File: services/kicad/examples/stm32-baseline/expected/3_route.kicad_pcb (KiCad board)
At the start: 2 copper layers, 50.3 x 37.7 mm, 17 parts, among them J1 5V, U1 STM32F103C8T6, U2 AMS1117-3.3

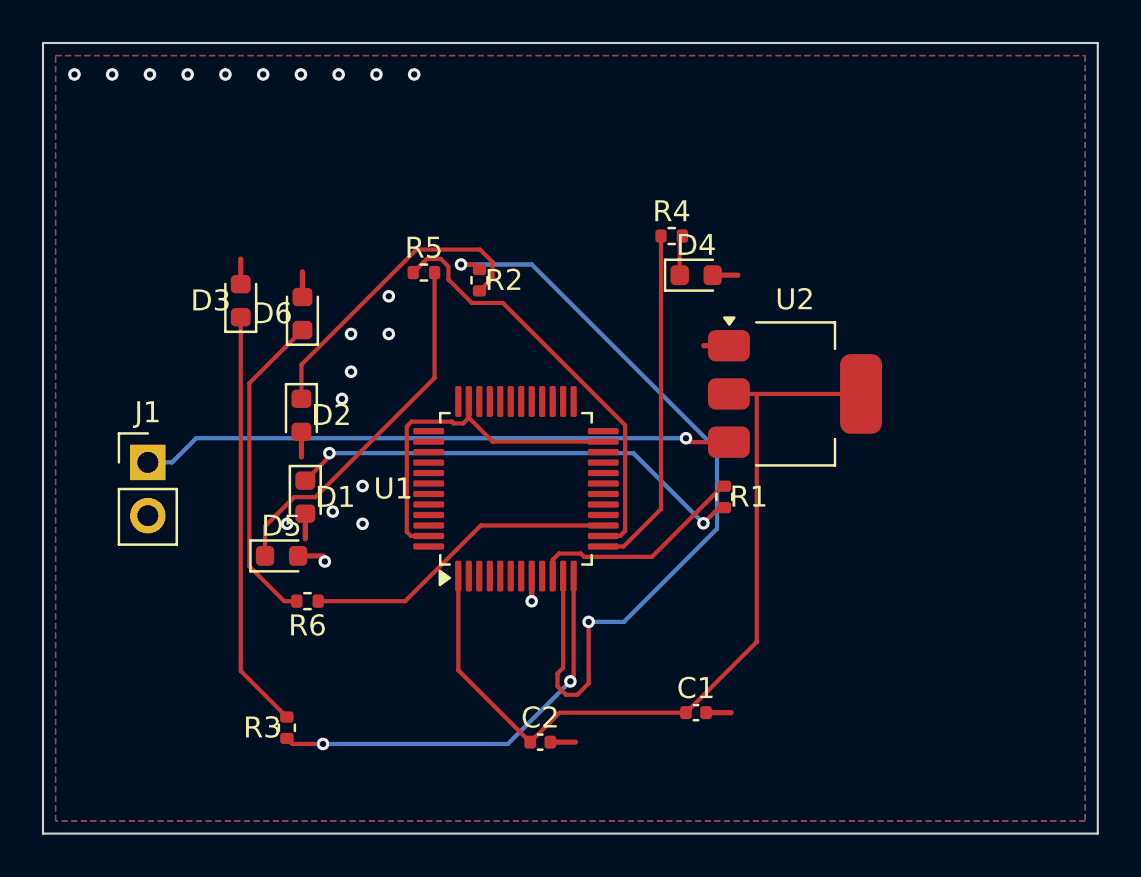
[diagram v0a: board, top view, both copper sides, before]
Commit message: feat(kicad): placement pro et routage 100 % fabricable sur les 16 cartes -- integration sur main (#164)
Branche d'integration coupee depuis origin/main (fab2a82, PR #162) : les
fichiers cles de main etaient des instantanes de feat/placement-seed-snap-
bypass (routing.py = 7981019, placement.py = 437a8b4...). On reprend donc
l'arbre entier de cette branche (345 commits, dernier 9f48667) et on y
conserve ce que main seul apportait :
- tools/verrou_routage.py + son test : « 6,2 Go par routage » rectifie
  (0,2 Go mesure ; c'est la concurrence qui emballe la memoire) ;
- tests/test_driver_llm_resync.py ;
- CLAUDE.md, PLAN.md, DECISIONS.md : fusion a trois voies, les sections
  des deux lignes conservees (2026-09-05 conteneur/verrou, 2026-09-07
  parcours asynchrone et chaine du driver, 2026-09-09/10 lecons).
Les skills *-delegate restent supprimes (remplaces le 2026-08-30).

Contenu : banc en deux phases (placement valide puis routage gele), snap
sur les regles natives, repli GND cible, journal Freerouting incremental,
horloge sans progres, via d'echappement vers le plan principal,
serigraphie degagee ; 16 cartes livrees a 100 %, 0 erreur DRC.

Verification : pytest services/kicad 1805 passed, 16 skipped ;
pnpm type-check 8/8.


Claude-Session: https://claude.ai/code/session_01TnMqm4La2CxQHHB5K8aSSV

Co-authored-by: Claude Fable 5.1 <noreply@anthropic.com>
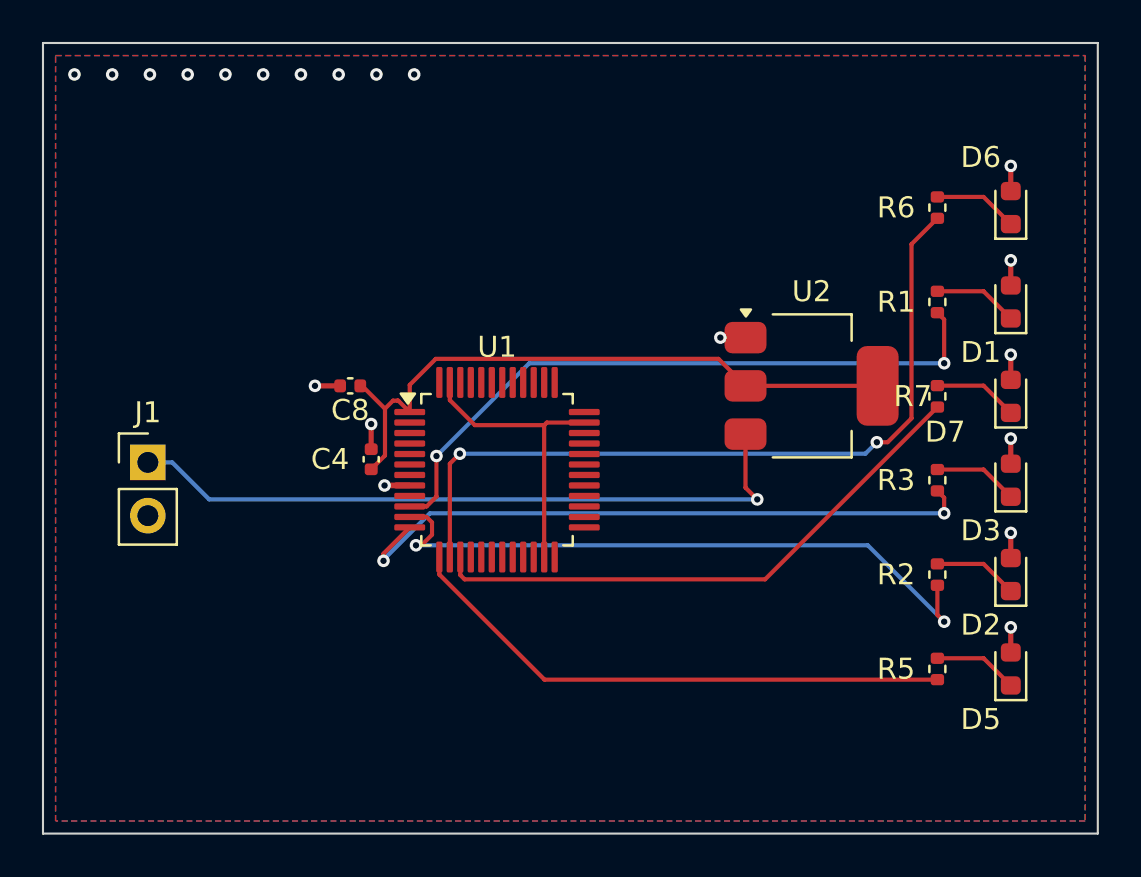
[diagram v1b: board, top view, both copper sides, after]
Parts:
- removed C1, C2: 100nF, C_0402_1005Metric
- removed D4: LED, LED_0603_1608Metric
- removed R4: 330, R_0402_1005Metric
- added C4: 100nF, C_0402_1005Metric, F.Cu at (139.0, 106.0)
- added C8: 100nF, C_0402_1005Metric, F.Cu at (138.0, 102.5)
- added D7: LED, LED_0603_1608Metric, F.Cu at (169.5, 103.0)
- added R7: 330, R_0402_1005Metric, F.Cu at (166.0, 103.0)
- moved D3 37.7 mm to (169.5, 107.0)
- moved R6 35.4 mm to (166.0, 94.0), turned to 90 degrees
- moved D5 35.2 mm to (169.5, 116.0), turned to 90 degrees
- moved D1 34.9 mm to (169.5, 98.5), turned to 90 degrees
- moved D2 34.7 mm to (169.5, 111.5), turned to 90 degrees
- moved D6 34.2 mm to (169.5, 94.0)
- moved R3 33.2 mm to (166.0, 107.0)
- moved R5 30.9 mm to (166.0, 116.0), turned to 90 degrees
- moved R2 26.0 mm to (166.0, 111.5), turned to 90 degrees
- moved R1 13.8 mm to (166.0, 98.5), turned to 90 degrees
- moved U1 1.28 mm to (145.0, 106.5), turned to 0 degrees
- moved U2 0.88 mm to (160.0, 102.5)
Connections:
- D5 pad 1: LED6 -> LED5
- D6 pad 1: LED7 -> LED6
- R5 pad 1: GPIO6 -> GPIO5
- R5 pad 2: LED6 -> LED5
- R6 pad 1: GPIO7 -> GPIO6
- R6 pad 2: LED7 -> LED6
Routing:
- net GPIO1: track 10.5 -> 32.0 mm, vias 0 -> 2
- net LED1: track 22.3 -> 4.04 mm, vias 2 -> 0
- net GPIO6: track 20.2 -> 37.4 mm, vias 0 -> 2
- net LED3: track 20.0 -> 4.04 mm
- net LED6: track 17.5 -> 4.04 mm
- net GPIO7: track 15.1 -> 27.1 mm
- net LED7: track 15.3 -> 4.04 mm
- net GPIO3: track 20.0 -> 31.0 mm
- net LED2: track 14.9 -> 4.04 mm
- net GPIO5: track 16.5 -> 26.7 mm
- net +3V3: track 40.2 -> 31.0 mm
- net GPIO2: track 38.8 -> 31.3 mm
- net VIN: track 28.3 -> 33.1 mm
- net Net-(U1-23): track 17.0 -> 14.1 mm
- net GND: track 12.0 -> 14.4 mm, vias 21 -> 20
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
